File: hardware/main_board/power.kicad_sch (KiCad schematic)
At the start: 0 parts

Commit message: WIP: power module
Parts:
- added C1: 47n, symbol Device:C_Small
- added C2: 20u, symbol Device:C_Small
- added C3: 4u7, symbol Device:C_Small
- added D1: LED, symbol Device:LED
- added J1: USB_C_Receptacle_USB2.0, symbol Connector:USB_C_Receptacle_USB2.0
- added R1: 2K2, symbol Device:R_Small
- added U1: BQ24195RGER, Project_Footprints:RGE0024H, symbol Project_Components:BQ24195RGER
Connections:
- new net: C1.1, U1.19 (SW), U1.20 (SW)
- new net: C1.2, U1.21 (BTST)
- new net: D1.1 (K), R1.1
- new net: R1.2, U1.4 (STAT)
- new net: J1.A6 (D+), J1.B6 (D+), U1.2 (D+)
- new net: C2.2, U1.23 (PMID)
- new net: J1.A7 (D-), J1.B7 (D-), U1.3 (D-)
- new net: J1.A4 (VBUS), J1.A9 (VBUS), J1.B4 (VBUS), J1.B9 (VBUS)
- new net GND: C2.1, C3.2, J1.A1 (GND), J1.A12 (GND), J1.B1 (GND), J1.B12 (GND), J1.S1 (SHIELD), U1.17 (PGND), U1.18 (PGND), U1.25 (PAD)
- new net REGN: C3.1, D1.2 (A), U1.22 (REGN)
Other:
- note added: "Charge Status"

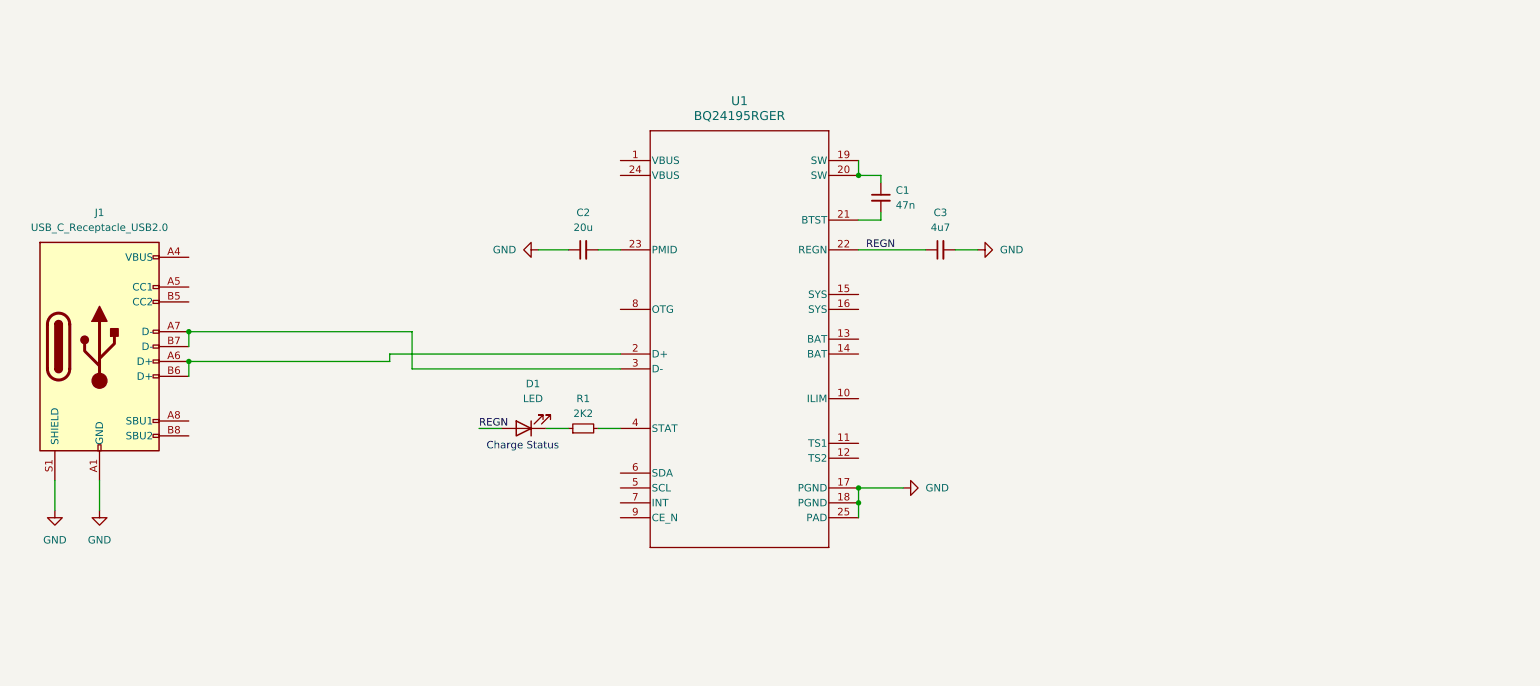
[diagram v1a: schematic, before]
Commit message: Update mainboard schematic to match breadboard
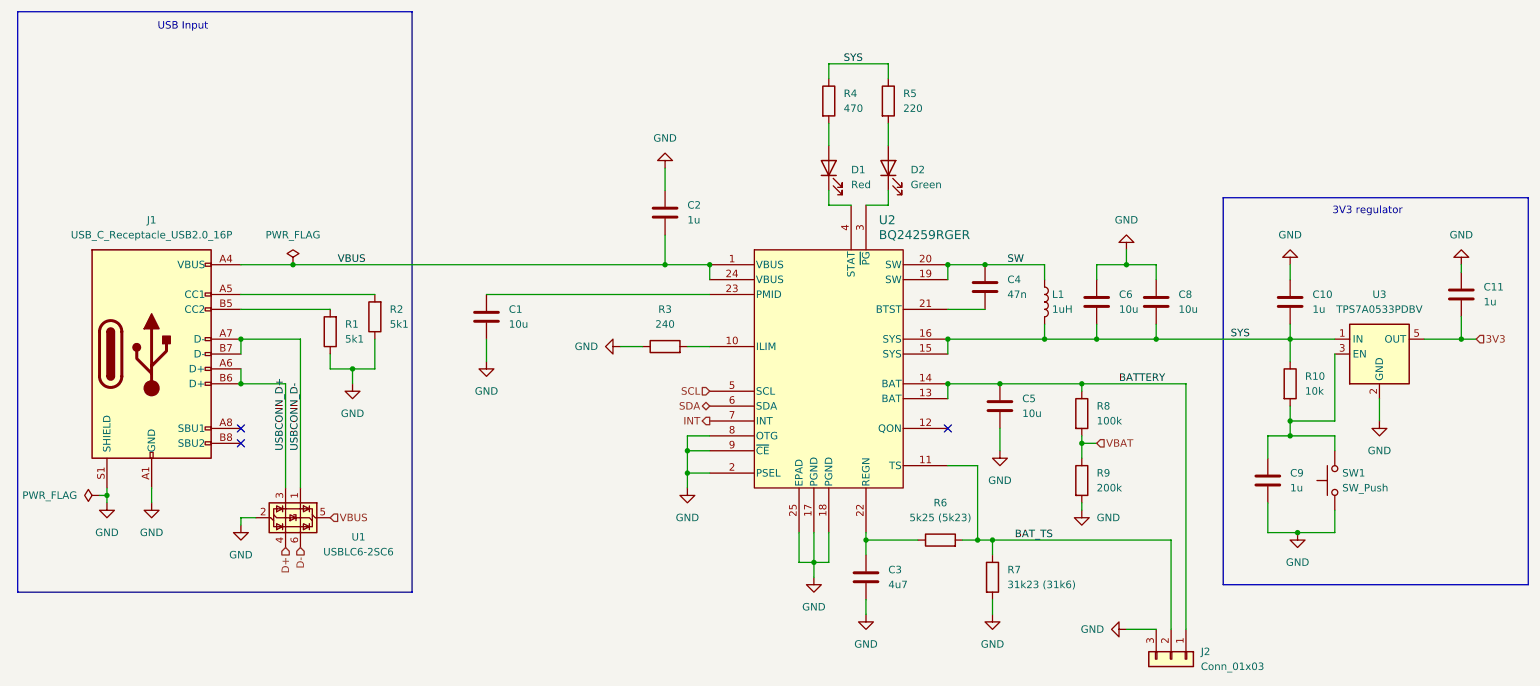
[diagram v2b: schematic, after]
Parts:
- removed C1: 47n, symbol Device:C_Small
- removed C2: 20u, symbol Device:C_Small
- removed C3: 4u7, symbol Device:C_Small
- removed J1: USB_C_Receptacle_USB2.0, symbol Connector:USB_C_Receptacle_USB2.0
- removed R1: 2K2, symbol Device:R_Small
- removed U1: BQ24195RGER, Project_Footprints:RGE0024H, symbol Project_Components:BQ24195RGER
- added C1, C5, C6, C8: 10u, Capacitor_SMD:C_0603_1608Metric, symbol Device:C
- added C10, C11, C2, C9: 1u, Capacitor_SMD:C_0402_1005Metric, symbol Device:C
- added C3: 4u7, Capacitor_SMD:C_0402_1005Metric, symbol Device:C
- added C4: 47n, Capacitor_SMD:C_0402_1005Metric, symbol Device:C
- added D2: Green, LED_SMD:LED_0603_1608Metric, symbol Device:LED
- added J1: USB_C_Receptacle_USB2.0_16P, Connector_USB:USB_C_Receptacle_GCT_USB4105-xx-A_16P_TopMnt_Horizontal, symbol Connector:USB_C_Receptacle_USB2.0_16P
- added J2: Conn_01x03, Connector_JST:JST_PH_S3B-PH-SM4-TB_1x03-1MP_P2.00mm_Horizontal, symbol Connector_Generic:Conn_01x03
- added L1: 1uH, Inductor_SMD:L_Murata_DFE201610P, symbol Device:L
- added R1, R2: 5k1, Resistor_SMD:R_0402_1005Metric, symbol Device:R
- added R10: 10k, Resistor_SMD:R_0402_1005Metric, symbol Device:R
- added R3: 240, Resistor_SMD:R_0402_1005Metric, symbol Device:R
- added R4: 470, Resistor_SMD:R_0402_1005Metric, symbol Device:R
- added R5: 220, Resistor_SMD:R_0402_1005Metric, symbol Device:R
- added R6: 5k25 (5k23), Resistor_SMD:R_0402_1005Metric, symbol Device:R
- added R7: 31k23 (31k6), Resistor_SMD:R_0402_1005Metric, symbol Device:R
- added R8: 100k, Resistor_SMD:R_0402_1005Metric, symbol Device:R
- added R9: 200k, Resistor_SMD:R_0402_1005Metric, symbol Device:R
- added SW1: SW_Push, Button_Switch_SMD:SW_SPST_PTS810, symbol Switch:SW_Push
- added U1: USBLC6-2SC6, Package_TO_SOT_SMD:SOT-23-6, symbol Power_Protection:USBLC6-2SC6
- added U2: BQ24259RGER, RGE24_2P7X2P7_TEX, symbol Project_Symbols:BQ24259RGER
- added U3: TPS7A0533PDBV, Package_TO_SOT_SMD:SOT-23-5, symbol Regulator_Linear:TPS7A0533PDBV
- D1: value LED -> Red; footprint (none) -> LED_SMD:LED_0603_1608Metric; JLCPCB (none) -> C2286
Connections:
- net GND: now also C1.2, C10.1, C11.1, C2.1, C3.2, C5.2, C6.1, C8.1, C9.2, J1.A1 (GND), J1.A12 (GND), J1.B1 (GND), J1.B12 (GND), J1.S1 (SHIELD), J2.3 (Pin_3), R1.1, R2.1, R3.1, R7.2, R9.2, SW1.1, U1.2 (GND), U2.17 (PGND), U2.18 (PGND), U2.2 (PSEL), U2.25 (EPAD), U2.8 (OTG), U2.9 (~{CE}), U3.2 (GND)
- net at D1.1 (K): now also U2.4 (STAT)
- net REGN: no longer names the net of D1.2 (A)
- net REGN: now also R4.2
- new net: C9.1, R10.2, SW1.2, U3.3 (EN)
- new net: C3.1, R6.1, U2.22 (REGN)
- new net: J1.A5 (CC1), R2.2
- new net: J1.B5 (CC2), R1.2
- new net: C4.2, U2.21 (BTST)
- new net: R3.2, U2.10 (ILIM)
- new net: C1.1, U2.23 (PMID)
- new net: D2.1 (K), U2.3 (~{PG})
- new net: D2.2 (A), R5.2
- new net 3V3: C11.2, U3.5 (OUT)
- new net BATTERY: C5.1, J2.1 (Pin_1), R8.1, U2.13 (BAT), U2.14 (BAT)
- new net BAT_TS: J2.2 (Pin_2), R6.2, R7.1, U2.11 (TS)
- new net D+: U1.4 (I/O2)
- new net D-: U1.6 (I/O1)
- new net INT: U2.7 (INT)
- new net SCL: U2.5 (SCL)
- new net SDA: U2.6 (SDA)
- new net SW: C4.1, L1.1, U2.19 (SW), U2.20 (SW)
- new net SYS: C10.2, C6.2, C8.2, L1.2, R10.1, R4.1, R5.1, U2.15 (SYS), U2.16 (SYS), U3.1 (IN)
- new net USBCONN_D+: J1.A6 (D+), J1.B6 (D+), U1.3 (I/O2)
- new net USBCONN_D-: J1.A7 (D-), J1.B7 (D-), U1.1 (I/O1)
- new net VBAT: R8.2, R9.1
- new net VBUS: C2.2, J1.A4 (VBUS), J1.A9 (VBUS), J1.B4 (VBUS), J1.B9 (VBUS), U1.5 (VBUS), U2.1 (VBUS), U2.24 (VBUS)
- no-connect marks 0 -> 3
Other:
- note added: "3V3 regulator"
- note added: "USB Input"
- note removed: "Charge Status"
- title: Power components -> Power subsystem

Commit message: Add probe connector
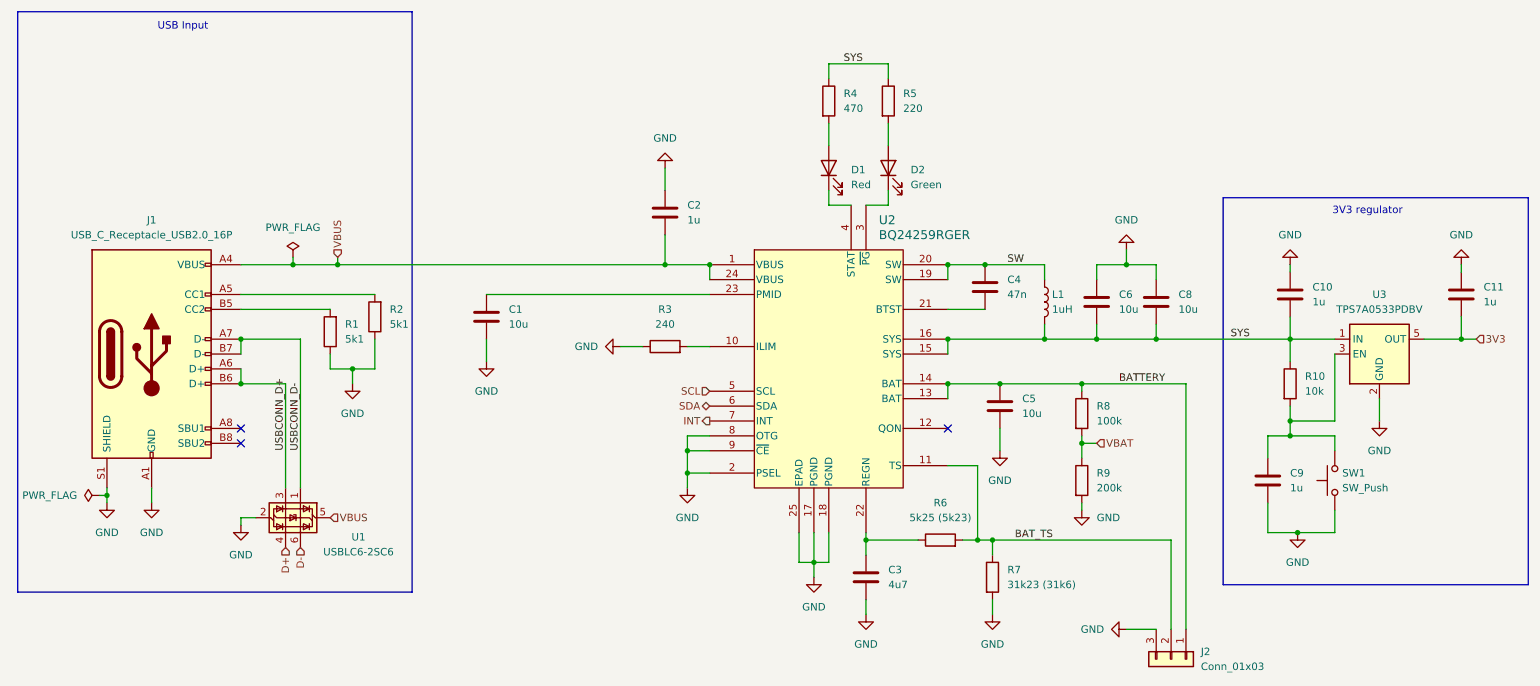
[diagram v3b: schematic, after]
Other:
- moved on the sheet: C10
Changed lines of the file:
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@@
 	)
 	(junction
+		(at 76.2 82.55)
+		(diameter 0)
+		(color 0 0 0 0)
+	)
+	(junction
 		(at 267.97 95.25)
 		(diameter 0)
@@
 	(wire
 		(pts
-			(xy 68.58 82.55) (xy 132.08 82.55)
+			(xy 68.58 82.55) (xy 76.2 82.55)
 		)
 		(stroke
@@
 	(wire
 		(pts
-			(xy 238.76 82.55) (xy 238.76 85.09)
+			(xy 238.76 82.55) (xy 238.76 83.82)
 		)
 		(stroke
@@
 	(wire
 		(pts
-			(xy 238.76 92.71) (xy 238.76 95.25)
+			(xy 238.76 91.44) (xy 238.76 95.25)
 		)
 		(stroke
@@
 	(wire
 		(pts
+			(xy 76.2 81.28) (xy 76.2 82.55)
+		)
+		(stroke
+			(width 0)
+			(type default)
+		)
+	)
+	(wire
+		(pts
 			(xy 196.85 95.25) (xy 196.85 92.71)
 		)
@@
 	(wire
 		(pts
+			(xy 76.2 82.55) (xy 132.08 82.55)
+		)
+		(stroke
+			(width 0)
+			(type default)
+		)
+	)
+	(wire
+		(pts
 			(xy 44.45 120.65) (xy 44.45 123.19)
 		)
@@
 	(wire
 		(pts
+			(xy 68.58 81.28) (xy 68.58 82.55)
+		)
+		(stroke
+			(width 0)
+			(type default)
+		)
+	)
+	(wire
+		(pts
 			(xy 238.76 111.76) (xy 246.38 111.76)
 		)
@@
 		)
 	)
-	(label "VBUS"
-		(at 76.2 82.55 0)
-		(effects
-			(font
-				(size 1.27 1.27)
-			)
-			(justify left bottom)
-		)
-	)
 	(label "SYS"
 		(at 228.6 95.25 0)
@@
 		)
 	)
+	(hierarchical_label "VBUS"
+		(shape input)
+		(at 76.2 81.28 90)
+		(effects
+			(font
+				(size 1.27 1.27)
+			)
+			(justify left)
+		)
+	)
 	(hierarchical_label "SCL"
 		(shape input)
@@
 	(symbol
 		(lib_id "power:PWR_FLAG")
-		(at 68.58 82.55 0)
+		(at 68.58 81.28 0)
 		(unit 1)
 		(exclude_from_sim no)
@@
 		(fields_autoplaced yes)
 		(property "Reference" "#FLG01"
-			(at 68.58 80.645 0)
+			(at 68.58 79.375 0)
 			(effects
 				(font
@@
 		)
 		(property "Value" "PWR_FLAG"
-			(at 68.58 77.47 0)
+			(at 68.58 76.2 0)
 			(effects
 				(font
@@
 		)
 		(property "Footprint" ""
-			(at 68.58 82.55 0)
+			(at 68.58 81.28 0)
 			(effects
 				(font
@@
 		)
 		(property "Datasheet" "~"
-			(at 68.58 82.55 0)
+			(at 68.58 81.28 0)
 			(effects
 				(font
@@
 		)
 		(property "Description" "Special symbol for telling ERC where power comes from"
-			(at 68.58 82.55 0)
+			(at 68.58 81.28 0)
 			(effects
 				(font
@@
 	(symbol
 		(lib_id "Device:C")
-		(at 238.76 88.9 0)
+		(at 238.76 87.63 0)
 		(unit 1)
 		(exclude_from_sim no)
@@
 		(fields_autoplaced yes)
 		(property "Reference" "C10"
-			(at 242.57 87.6299 0)
+			(at 242.57 86.3599 0)
 			(effects
 				(font
@@
 		)
 		(property "Value" "1u"
-			(at 242.57 90.1699 0)
+			(at 242.57 88.8999 0)
 			(effects
 				(font
@@
 		)
 		(property "Footprint" "Capacitor_SMD:C_0402_1005Metric"
-			(at 239.7252 92.71 0)
+			(at 239.7252 91.44 0)
 			(effects
 				(font
@@
 		)
 		(property "Datasheet" "~"
-			(at 238.76 88.9 0)
+			(at 238.76 87.63 0)
 			(effects
 				(font
@@
 		)
 		(property "Description" "Unpolarized capacitor"
-			(at 238.76 88.9 0)
+			(at 238.76 87.63 0)
 			(effects
 				(font
@@
 		)
 		(property "JLCPCB" "C52923"
-			(at 238.76 88.9 0)
+			(at 238.76 87.63 0)
 			(effects
 				(font

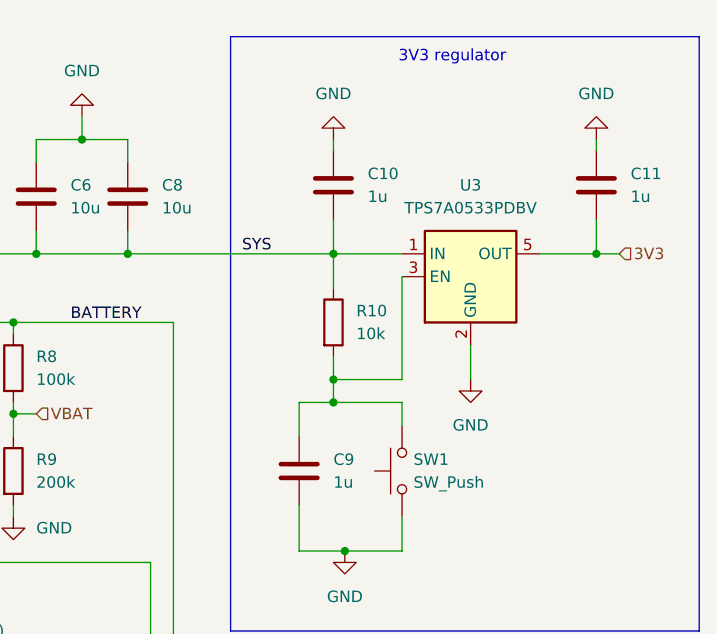
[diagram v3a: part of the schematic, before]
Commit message: Add daughter board connector
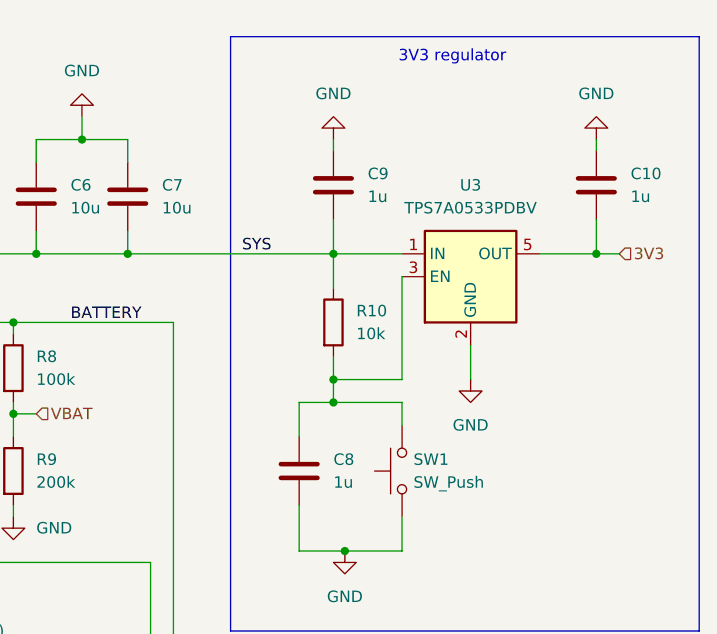
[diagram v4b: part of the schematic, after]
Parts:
- U2: footprint RGE24_2P7X2P7_TEX -> Project_Footprints:RGE24_2P7X2P7_TEX
- renumbered C11 to C10, C8 to C7, C9 to C8, C10 to C9
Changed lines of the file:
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@@
 		(dnp no)
 		(fields_autoplaced yes)
-		(property "Reference" "#FLG03"
+		(property "Reference" "#FLG01"
 			(at 33.655 121.92 0)
 			(effects
@@
 			(project ""
 				(path "/e7586151-38a0-41a9-9cce-542cfb7665db/36d2f76b-6786-406f-96a1-52265f303dbc"
-					(reference "#FLG03")
+					(reference "#FLG01")
 					(unit 1)
 				)
@@
 		(dnp no)
 		(fields_autoplaced yes)
-		(property "Reference" "C11"
+		(property "Reference" "C10"
 			(at 271.78 86.3599 0)
 			(effects
@@
 			(project "main_board"
 				(path "/e7586151-38a0-41a9-9cce-542cfb7665db/36d2f76b-6786-406f-96a1-52265f303dbc"
-					(reference "C11")
+					(reference "C10")
 					(unit 1)
 				)
@@
 		(dnp no)
 		(fields_autoplaced yes)
-		(property "Reference" "C8"
+		(property "Reference" "C7"
 			(at 219.71 87.6299 0)
 			(effects
@@
 			(project "main_board"
 				(path "/e7586151-38a0-41a9-9cce-542cfb7665db/36d2f76b-6786-406f-96a1-52265f303dbc"
-					(reference "C8")
+					(reference "C7")
 					(unit 1)
 				)
@@
 		(dnp no)
 		(fields_autoplaced yes)
-		(property "Reference" "#FLG01"
+		(property "Reference" "#FLG02"
 			(at 68.58 79.375 0)
 			(effects
@@
 			(project ""
 				(path "/e7586151-38a0-41a9-9cce-542cfb7665db/36d2f76b-6786-406f-96a1-52265f303dbc"
-					(reference "#FLG01")
+					(reference "#FLG02")
 					(unit 1)
 				)
@@
 			)
 		)
-		(property "Footprint" "RGE24_2P7X2P7_TEX"
+		(property "Footprint" "Project_Footprints:RGE24_2P7X2P7_TEX"
 			(at 139.7 85.09 0)
 			(effects
@@
 		(dnp no)
 		(fields_autoplaced yes)
-		(property "Reference" "C9"
+		(property "Reference" "C8"
 			(at 238.76 118.1099 0)
 			(effects
@@
 			(project "main_board"
 				(path "/e7586151-38a0-41a9-9cce-542cfb7665db/36d2f76b-6786-406f-96a1-52265f303dbc"
-					(reference "C9")
+					(reference "C8")
 					(unit 1)
 				)
@@
 		(dnp no)
 		(fields_autoplaced yes)
-		(property "Reference" "C10"
+		(property "Reference" "C9"
 			(at 242.57 86.3599 0)
 			(effects
@@
 			(project "main_board"
 				(path "/e7586151-38a0-41a9-9cce-542cfb7665db/36d2f76b-6786-406f-96a1-52265f303dbc"
-					(reference "C10")
-					(unit 1)
-				)
+					(reference "C9")
+					(unit 1)
+				)
